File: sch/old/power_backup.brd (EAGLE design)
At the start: 56 x 35 mm, 34 parts, among them IC1 78L05SMD, IC2 ACS712-LC, K1 DS2Y-S-DC48V, T1 BC847, T2 BC847, T3 BC847

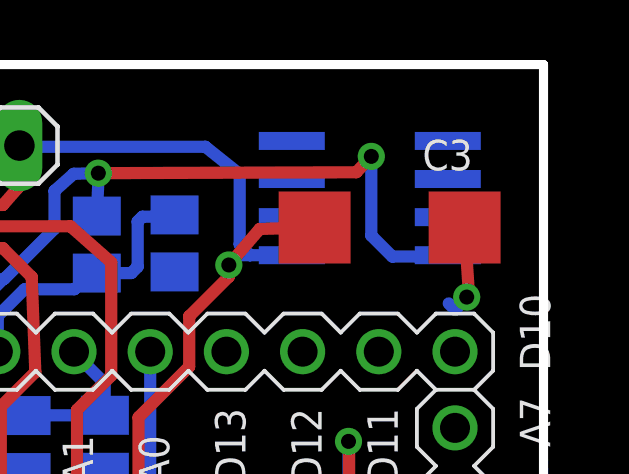
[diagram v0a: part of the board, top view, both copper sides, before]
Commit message: code example added
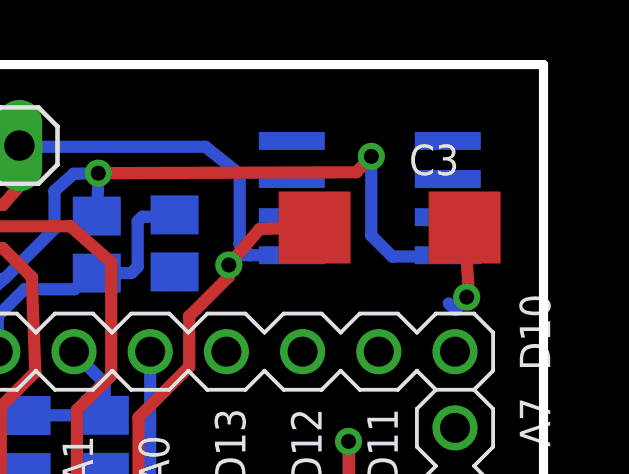
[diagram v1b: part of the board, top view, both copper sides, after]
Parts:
- C1: value (none) -> 1n
- C2: value (none) -> 100n
- R10, R7: value (none) -> 560
- R14, R16, R9: value (none) -> 100k
- R15, R17: value (none) -> 15k
- R6, R8: value (none) -> 10k
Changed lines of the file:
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@@
 <grid distance="1" unitdist="mm" unit="mm" style="lines" multiple="1" display="no" altdistance="0.01" altunitdist="mm" altunit="mm"/>
 <layers>
-<layer number="1" name="Top" color="4" fill="1" visible="no" active="yes"/>
+<layer number="1" name="Top" color="4" fill="1" visible="yes" active="yes"/>
 <layer number="2" name="Route2" color="1" fill="3" visible="no" active="no"/>
 <layer number="3" name="Route3" color="4" fill="3" visible="no" active="no"/>
@@
 <layer number="20" name="Dimension" color="15" fill="1" visible="yes" active="yes"/>
 <layer number="21" name="tPlace" color="7" fill="1" visible="yes" active="yes"/>
-<layer number="22" name="bPlace" color="7" fill="1" visible="no" active="yes"/>
+<layer number="22" name="bPlace" color="7" fill="1" visible="yes" active="yes"/>
 <layer number="23" name="tOrigins" color="15" fill="1" visible="yes" active="yes"/>
-<layer number="24" name="bOrigins" color="15" fill="1" visible="no" active="yes"/>
+<layer number="24" name="bOrigins" color="15" fill="1" visible="yes" active="yes"/>
 <layer number="25" name="tNames" color="7" fill="1" visible="yes" active="yes"/>
 <layer number="26" name="bNames" color="7" fill="1" visible="yes" active="yes"/>
@@
 <layer number="49" name="Reference" color="7" fill="1" visible="no" active="yes"/>
 <layer number="50" name="dxf" color="7" fill="1" visible="no" active="no"/>
-<layer number="51" name="tDocu" color="7" fill="1" visible="no" active="yes"/>
-<layer number="52" name="bDocu" color="7" fill="1" visible="no" active="yes"/>
+<layer number="51" name="tDocu" color="7" fill="1" visible="yes" active="yes"/>
+<layer number="52" name="bDocu" color="7" fill="1" visible="yes" active="yes"/>
 <layer number="56" name="wert" color="7" fill="1" visible="no" active="yes"/>
 <layer number="91" name="Nets" color="2" fill="1" visible="no" active="no"/>
@@
 <attribute name="VALUE" x="37.86" y="14.73" size="1.27" layer="28" rot="MR270"/>
 </element>
-<element name="R6" library="rcl" package="M0805" value="" x="45.08" y="18.12" smashed="yes" rot="MR180">
+<element name="R6" library="rcl" package="M0805" value="10k" x="45.08" y="18.12" smashed="yes" rot="MR180">
 <attribute name="NAME" x="44.21" y="20.59" size="1.27" layer="26" rot="MR180"/>
 <attribute name="VALUE" x="43.81" y="20.66" size="1.27" layer="28" rot="MR180"/>
 </element>
-<element name="R7" library="rcl" package="M0805" value="" x="48.04" y="13.5" smashed="yes" rot="MR270">
+<element name="R7" library="rcl" package="M0805" value="560" x="48.04" y="13.5" smashed="yes" rot="MR270">
 <attribute name="NAME" x="48.47" y="8.96" size="1.27" layer="26" rot="MR270"/>
 <attribute name="VALUE" x="50.58" y="14.77" size="1.27" layer="28" rot="MR270"/>
 </element>
-<element name="R8" library="rcl" package="M0805" value="" x="2.98" y="3.15" smashed="yes" rot="MR270">
+<element name="R8" library="rcl" package="M0805" value="10k" x="2.98" y="3.15" smashed="yes" rot="MR270">
 <attribute name="NAME" x="1.22" y="3.76" size="1.27" layer="26" rot="MR90"/>
 <attribute name="VALUE" x="5.52" y="4.42" size="1.27" layer="28" rot="MR270"/>
 </element>
-<element name="R9" library="rcl" package="M0805" value="" x="41.11" y="29" smashed="yes" rot="MR90">
-<attribute name="NAME" x="45.38" y="31.35" size="1.27" layer="26" rot="MR0"/>
+<element name="R9" library="rcl" package="M0805" value="100k" x="41.11" y="29" smashed="yes" rot="MR90">
+<attribute name="NAME" x="42.38" y="31.35" size="1.27" layer="26" rot="MR0"/>
 <attribute name="VALUE" x="38.57" y="27.73" size="1.27" layer="28" rot="MR90"/>
 </element>
@@
 <attribute name="VALUE" x="18.155" y="24.015" size="1.27" layer="28" rot="MR270"/>
 </element>
-<element name="R10" library="rcl" package="M0805" value="" x="53.73" y="13.5" smashed="yes" rot="MR270">
+<element name="R10" library="rcl" package="M0805" value="560" x="53.73" y="13.5" smashed="yes" rot="MR270">
 <attribute name="NAME" x="54.13" y="9.12" size="1.27" layer="26" rot="MR270"/>
 <attribute name="VALUE" x="56.27" y="14.77" size="1.27" layer="28" rot="MR270"/>
@@
 <attribute name="VALUE" x="12.355" y="1.043" size="1.27" layer="28" rot="MR0"/>
 </element>
-<element name="R14" library="rcl" package="M0805" value="" x="4.34" y="6.17" smashed="yes" rot="MR0">
+<element name="R14" library="rcl" package="M0805" value="100k" x="4.34" y="6.17" smashed="yes" rot="MR0">
 <attribute name="NAME" x="2.44" y="9.44" size="1.27" layer="26" rot="MR270"/>
 <attribute name="VALUE" x="5.61" y="3.63" size="1.27" layer="28" rot="MR0"/>
 </element>
-<element name="R15" library="rcl" package="M0805" value="" x="43.7" y="29.04" smashed="yes" rot="MR270">
-<attribute name="NAME" x="39.57" y="33.42" size="1.27" layer="26" rot="MR180"/>
+<element name="R15" library="rcl" package="M0805" value="15k" x="43.7" y="29.04" smashed="yes" rot="MR270">
+<attribute name="NAME" x="42.78" y="32.6" size="1.27" layer="26" rot="MR180"/>
 <attribute name="VALUE" x="46.24" y="30.31" size="1.27" layer="28" rot="MR270"/>
 </element>
-<element name="C1" library="rcl" package="C0805" value="" x="5.33" y="3.16" smashed="yes" rot="MR270">
+<element name="C1" library="rcl" package="C0805" value="1n" x="5.33" y="3.16" smashed="yes" rot="MR270">
 <attribute name="NAME" x="6.19" y="2.42" size="1.27" layer="26" rot="MR180"/>
 <attribute name="VALUE" x="7.87" y="4.43" size="1.27" layer="28" rot="MR270"/>
 </element>
-<element name="C2" library="rcl" package="C0805" value="" x="4.52" y="8.18" smashed="yes" rot="MR0">
+<element name="C2" library="rcl" package="C0805" value="100n" x="4.52" y="8.18" smashed="yes" rot="MR0">
 <attribute name="NAME" x="5.05" y="9.08" size="1.27" layer="26" rot="MR0"/>
 <attribute name="VALUE" x="5.79" y="5.64" size="1.27" layer="28" rot="MR0"/>
 </element>
-<element name="R16" library="rcl" package="M0805" value="" x="38.77" y="22.35" smashed="yes" rot="MR270">
+<element name="R16" library="rcl" package="M0805" value="100k" x="38.77" y="22.35" smashed="yes" rot="MR270">
 <attribute name="NAME" x="34.12" y="21.62" size="1.27" layer="26" rot="MR180"/>
 <attribute name="VALUE" x="41.31" y="23.62" size="1.27" layer="28" rot="MR270"/>
 </element>
-<element name="R17" library="rcl" package="M0805" value="" x="41.38" y="22.36" smashed="yes" rot="MR270">
+<element name="R17" library="rcl" package="M0805" value="15k" x="41.38" y="22.36" smashed="yes" rot="MR270">
 <attribute name="NAME" x="42.78" y="23.92" size="1.27" layer="26" rot="MR180"/>
 <attribute name="VALUE" x="43.92" y="23.63" size="1.27" layer="28" rot="MR270"/>
@@
 </element>
 <element name="C3" library="rcl" package="SMC_C" value="" x="50.87" y="29.57" smashed="yes">
-<attribute name="NAME" x="51.965" y="31.475" size="1.016" layer="25"/>
+<attribute name="NAME" x="51.515" y="31.315" size="1.016" layer="25"/>
 <attribute name="VALUE" x="48.965" y="27.03" size="1.016" layer="27"/>
 </element>
